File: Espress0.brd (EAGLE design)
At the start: 36.8 x 39.4 mm, 41 parts, among them CN1 4U#20329, Q2 reset, U1 AP2112K-3.3, U2 2MB Flash, U3 MCP73831T-2ACI/OT

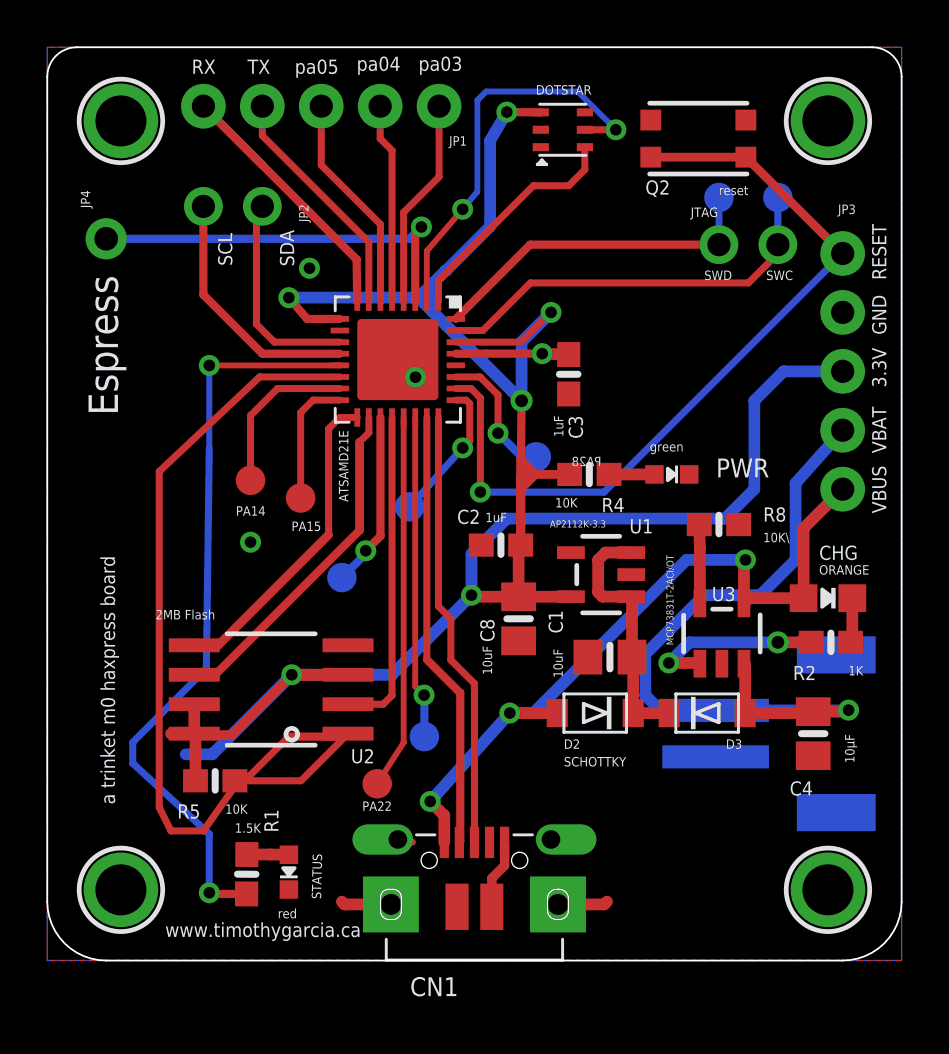
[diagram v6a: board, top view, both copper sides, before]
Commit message: Add files via upload
* Removed sharp & incorrect angles
* CS Select pin fix
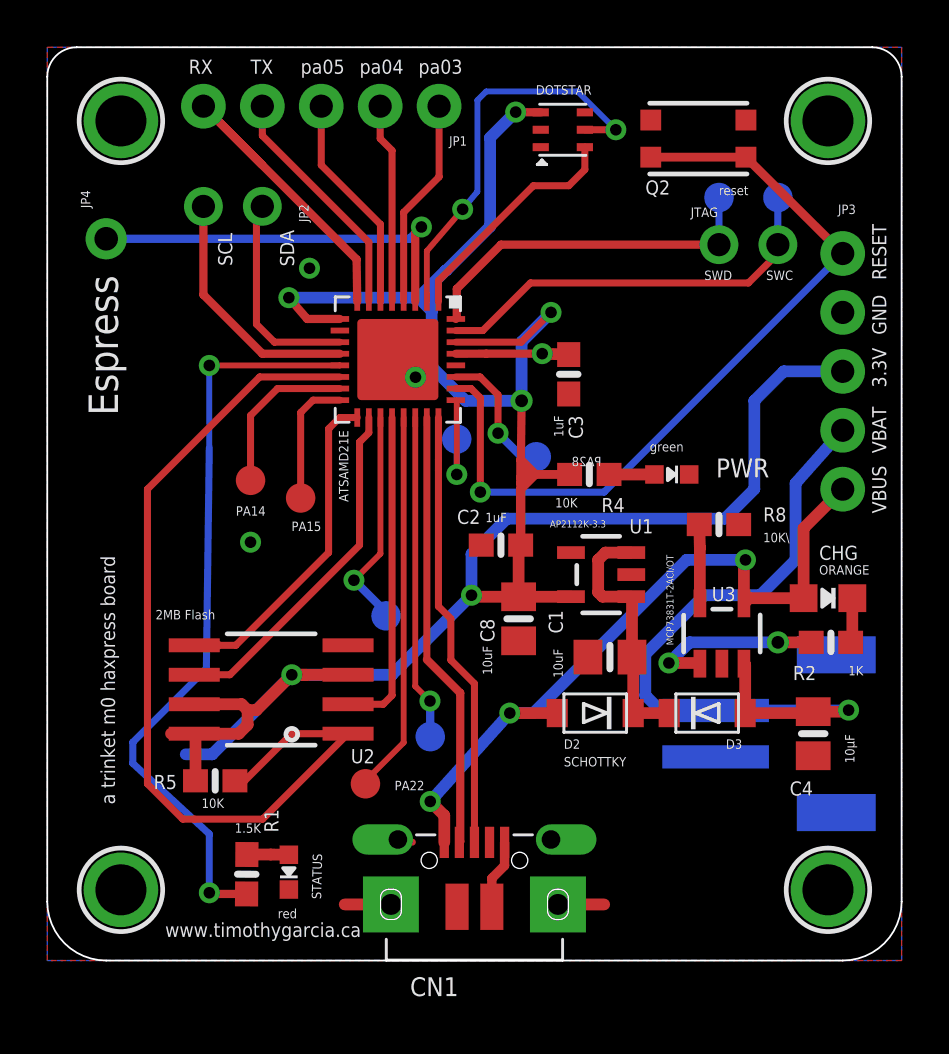
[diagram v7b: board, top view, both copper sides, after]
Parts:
- moved PA27 3.56 mm to (17.7, 22.5)
- moved PA18 2.52 mm to (14.6, 14.9)
- moved PA22 0.51 mm to (13.7, 7.62)
- moved PA23 0.25 mm to (16.5, 9.65)
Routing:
- net 3.3V: track 104.4 -> 107.2 mm
- net N$14: track 7.59 -> 9.60 mm
- net N$16: track 6.11 -> 4.74 mm
- net PA17D_FLASHSCK: track 14.7 -> 16.0 mm
- net SWD: track 14.7 -> 15.4 mm
- net PA16D_FLASHMOSI: track 13.8 -> 14.5 mm
